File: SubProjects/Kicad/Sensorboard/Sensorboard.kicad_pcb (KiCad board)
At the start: 2 copper layers, 60 x 44 mm, 15 parts, among them P1 ToyRaceCar_V2_REV3_J4, P2 ToyRaceCar_V2_REV3_J3, P3 ToyRaceCar_V2_REV3_J2, P4 ToyRaceCar_V2_REV3_J1, P5 MPU-6050, P6 ToyRaceCar_V2_REV3_J5, P7 CNY70, Q1 BSS138, Q2 BSS138

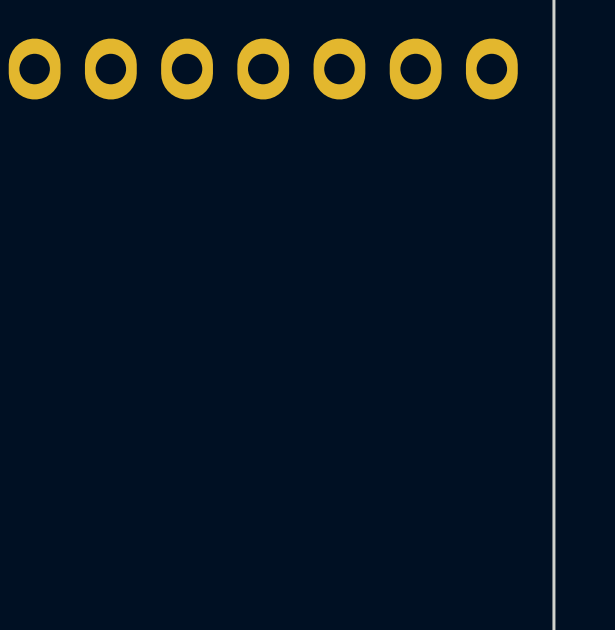
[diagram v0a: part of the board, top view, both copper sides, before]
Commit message: Added another connector for the hall sensor
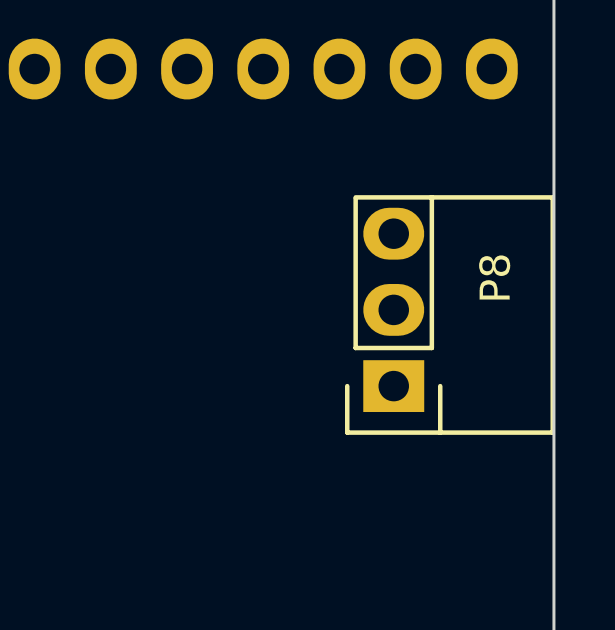
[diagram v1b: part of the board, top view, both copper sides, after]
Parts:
- added P8: SS495A, Sensorboard:KK254-3, F.Cu at (193.7, 113.5)
- P7: footprint Sensorboard:KK254 -> Sensorboard:KK254-4

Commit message: Nearly final design. Just missing the mounting holes
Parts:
- added R10: 3K3, Resistors_SMD:R_0805_HandSoldering, B.Cu at (166.0, 103.0)
- added R11: 10K, Resistors_SMD:R_0805_HandSoldering, B.Cu at (155.2, 92.1)
- added R7: 6K8, Resistors_SMD:R_0805_HandSoldering, B.Cu at (161.8, 104.5)
- added R8: 20K, Resistors_SMD:R_0805_HandSoldering, B.Cu at (151.9, 109.9)
- added R9: 6K8, Resistors_SMD:R_0805_HandSoldering, B.Cu at (156.6, 111.3)
- added RV1: 10K, Potentiometers:Potentiometer_Bourns_3006P_Angular_ScrewFront, F.Cu at (163.7, 110.6)
- added U1: AD623AN, Housings_DIP:DIP-8__300, F.Cu at (172.3, 103.0)
- added U2: LM311N, Housings_DIP:DIP-8__300, F.Cu at (155.2, 101.9)
- P8: footprint Sensorboard:KK254-3 -> Pin_Headers:Pin_Header_Angled_1x03
- R1, R2, R3, R4: footprint Resistors_SMD:R_0603_HandSoldering -> Resistors_SMD:R_0805_HandSoldering
- R5: value 22K -> 20K; footprint Resistors_SMD:R_0603_HandSoldering -> Resistors_SMD:R_0805_HandSoldering
- R6: value 560R -> 150R; footprint Resistors_SMD:R_0603_HandSoldering -> Resistors_SMD:R_0805_HandSoldering
- moved R3 26.2 mm to (140.3, 118.0)
- moved P4 25.1 mm to (131.7, 87.2)
- moved P2 25.1 mm to (121.5, 125.3)
- moved P6 25.1 mm to (121.5, 110.1)
- moved P7 25.1 mm to (124.7, 85.9)
- moved P1 25.1 mm to (154.5, 125.3)
- moved P3 25.1 mm to (154.5, 87.2)
- moved Q1 25.1 mm to (142.4, 97.3)
- moved Q2 25.1 mm to (136.4, 97.3)
- moved R1 25.1 mm to (145.0, 95.0)
- moved R5 25.1 mm to (128.6, 87.4)
- moved R6 25.1 mm to (130.4, 93.1)
- moved P5 25.1 mm to (131.4, 95.6)
- moved R4 25.0 mm to (145.0, 99.9)
- moved R2 24.7 mm to (139.4, 95.0)
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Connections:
- P2 pad 7: Net-(P2-Pad7) -> /PD6
- P8 pad 2: Net-(P8-Pad2) -> /+5V
- P8 pad 3: Net-(P8-Pad3) -> /GND
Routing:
- net /+5V: track 83.9 -> 164.6 mm, vias 0 -> 2
- net /GND: track 46.0 -> 120.9 mm, vias 0 -> 4
- net /PD6: track 0.00 -> 48.2 mm, vias 0 -> 2
- net /SDA(5V): track 2.62 -> 29.6 mm, vias 0 -> 1
- net /AD623AN_Out: track 0.00 -> 26.4 mm, vias 0 -> 2
- net Net-(R7-Pad1): track 0.00 -> 13.9 mm
- net Net-(P8-Pad1): track 0.00 -> 9.82 mm
- net Net-(RV1-Pad2): track 0.00 -> 6.35 mm
- net /SCL(5V): track 38.6 -> 44.2 mm
- net Net-(R10-Pad2): track 0.00 -> 4.97 mm
- net Net-(R10-Pad1): track 0.00 -> 4.94 mm
- net /SCL(3.3V): track 13.4 -> 13.9 mm

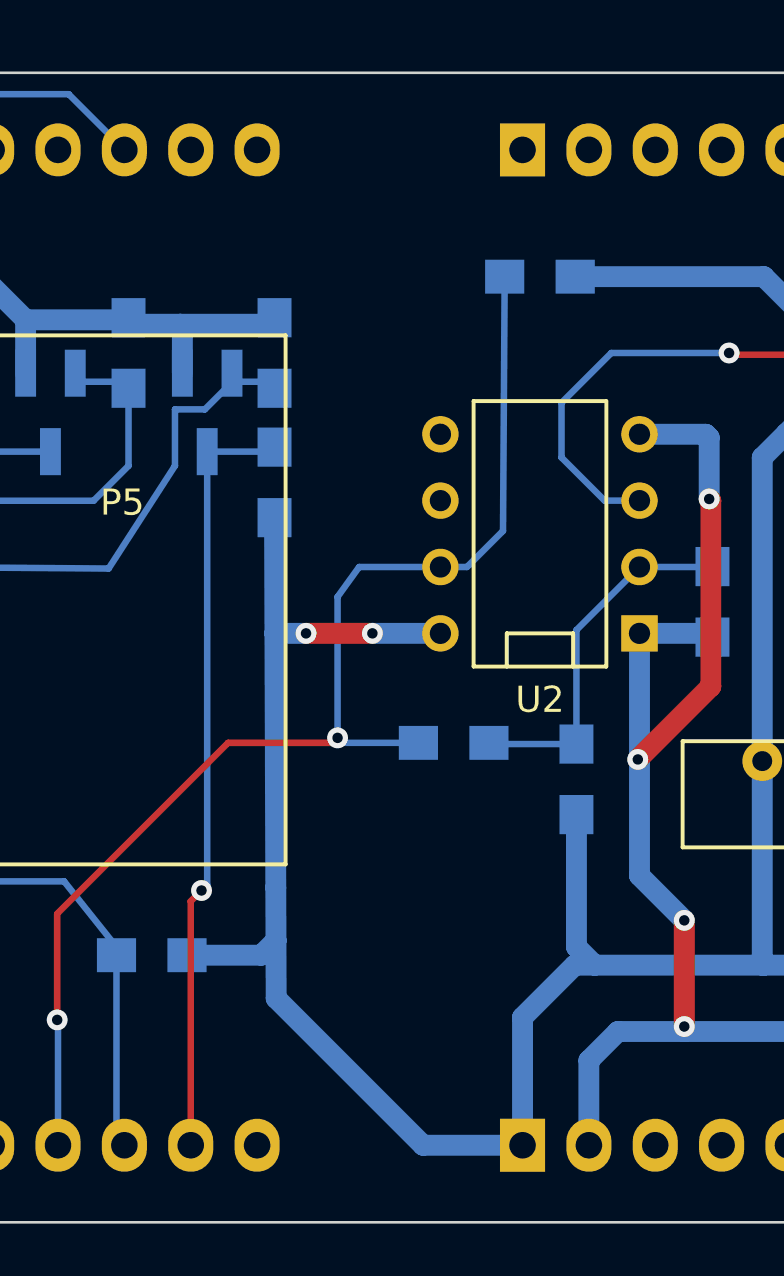
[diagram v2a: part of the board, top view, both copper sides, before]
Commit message: Added two 2.5mm mounting holes. We need to check if that is the actual size, but atleast they are in the correct position now.
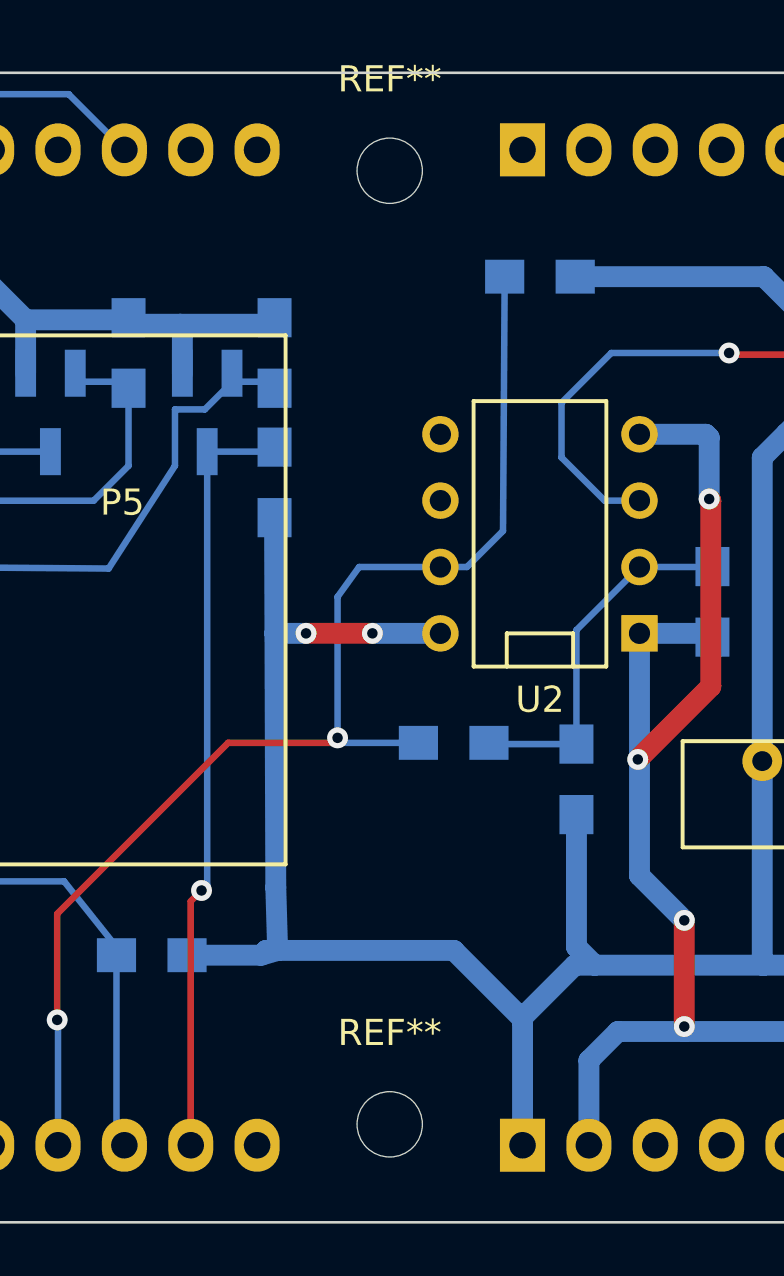
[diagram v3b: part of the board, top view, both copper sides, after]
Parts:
- added REF**: MountingHole_2-5mm, Mounting_Holes:MountingHole_2-5mm, F.Cu at (149.4, 124.5)
- added REF**: MountingHole_2-5mm, Mounting_Holes:MountingHole_2-5mm, F.Cu at (149.4, 88.0)
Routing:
- net /+5V: track 164.6 -> 162.4 mm

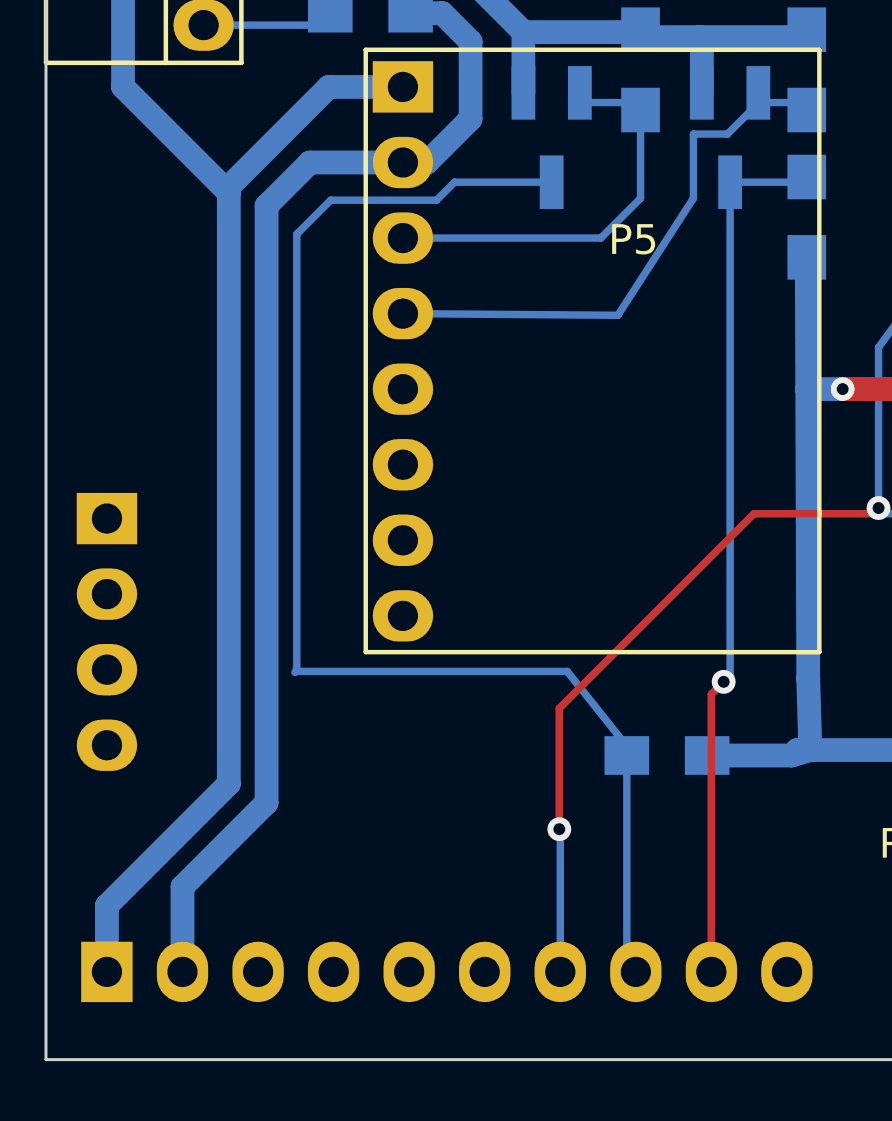
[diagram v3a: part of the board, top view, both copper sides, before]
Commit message: Added a connection from the int pin on the mpu6050 to the int0 on the microcontroller. If we need it at some point.
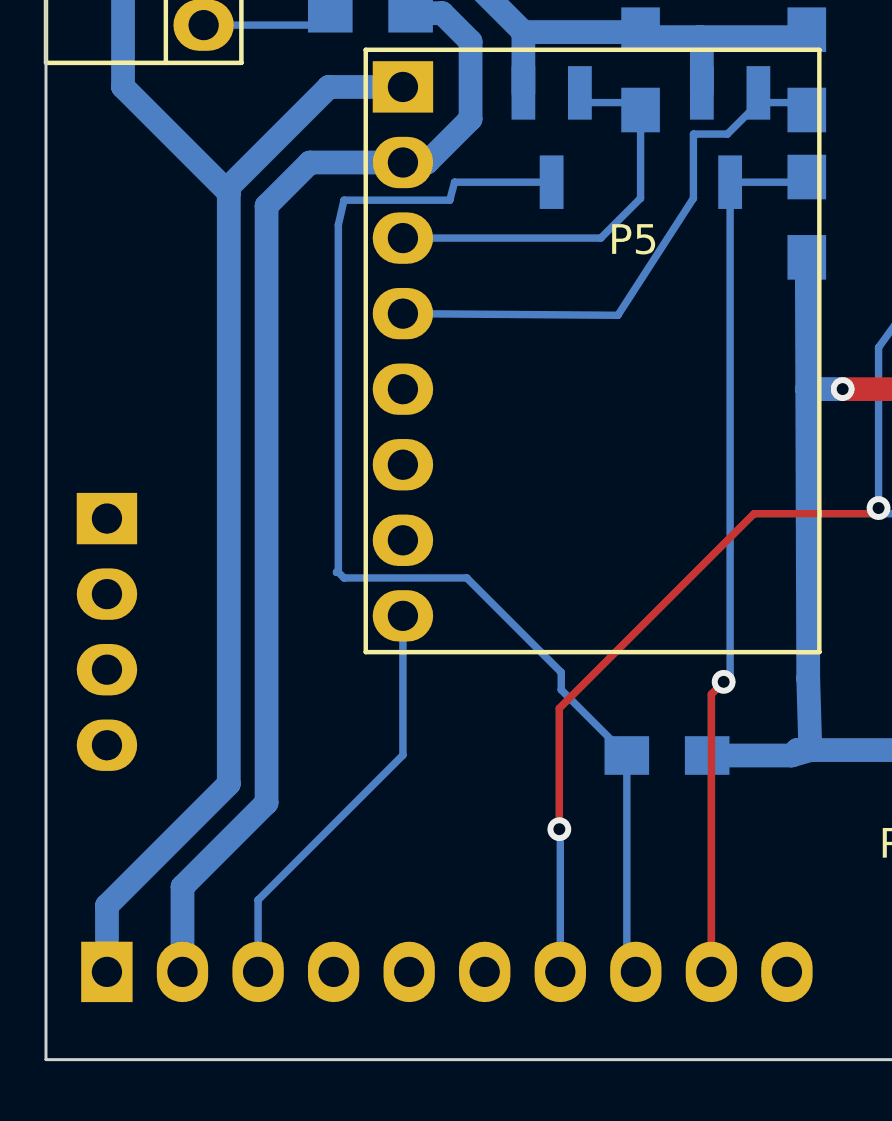
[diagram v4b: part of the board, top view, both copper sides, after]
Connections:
- P5 pad 8: Net-(P5-Pad8) -> Net-(P2-Pad3)
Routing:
- net Net-(P2-Pad3): track 0.00 -> 14.0 mm
- net /SCL(5V): track 44.2 -> 40.1 mm

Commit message: cleanup
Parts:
- removed the REF** at (149.4, 124.5)
- removed the REF** at (149.4, 88.0)
- added REF**: MountingHole_3mm, Sensorboard:MountingHole_3mm-7mm, F.Cu at (149.4, 88.0)
- added REF**: MountingHole_3mm, Sensorboard:MountingHole_3mm-7mm, F.Cu at (149.4, 124.5)
